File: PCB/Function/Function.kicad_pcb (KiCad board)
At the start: 2 copper layers, 101.6 x 152.4 mm, 12 parts

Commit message: Update Function.kicad_sch
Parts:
- removed J**11, J**12: Pomona_1581, 5Y:Pomona-1581
- moved J**3 56.8 mm to (38.1, 63.5)
- moved J**7 56.8 mm to (38.1, 88.9)
- moved J**4 56.8 mm to (63.5, 63.5)
- moved J**8 56.8 mm to (63.5, 88.9)
- moved J**5 50.8 mm to (88.9, 63.5)
- moved J**9 50.8 mm to (88.9, 88.9)
- moved J**10 50.8 mm to (114.3, 88.9)
- moved J**6 50.8 mm to (114.3, 63.5)
- moved J**2 25.4 mm to (88.9, 38.1)
- moved J**1 25.4 mm to (63.5, 38.1)
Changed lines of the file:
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@@
 	(net 9 "unconnected-(J**9-Pad1)")
 	(net 10 "unconnected-(J**10-Pad1)")
-	(net 11 "unconnected-(J**11-Pad1)")
-	(net 12 "unconnected-(J**12-Pad1)")
-	(footprint "5Y:Pomona-1581"
-		(layer "F.Cu")
-		(at 114.3 63.5)
+	(footprint "5Y:Pomona-1581"
+		(layer "F.Cu")
+		(at 63.5 88.9)
 		(descr "4mm banana connector")
 		(tags "jack")
@@
 	(footprint "5Y:Pomona-1581"
 		(layer "F.Cu")
-		(at 38.1 63.5)
+		(at 88.9 63.5)
 		(descr "4mm banana connector")
 		(tags "jack")
@@
 	(footprint "5Y:Pomona-1581"
 		(layer "F.Cu")
-		(at 63.5 88.9)
+		(at 114.3 88.9)
 		(descr "4mm banana connector")
 		(tags "jack")
@@
 	(footprint "5Y:Pomona-1581"
 		(layer "F.Cu")
-		(at 63.5 38.1)
+		(at 88.9 38.1)
 		(descr "4mm banana connector")
 		(tags "jack")
@@
 	(footprint "5Y:Pomona-1581"
 		(layer "F.Cu")
-		(at 88.9 88.9)
-		(descr "4mm banana connector")
-		(tags "jack")
-		(property "Reference" "J**11"
-			(at 0 -0.5 0)
-			(unlocked yes)
-			(layer "F.SilkS")
-			(hide yes)
-			(effects
-				(font
-					(size 1 1)
-					(thickness 0.1)
-				)
-			)
-		)
-		(property "Value" "Pomona_1581"
-			(at 0 1 0)
-			(unlocked yes)
-			(layer "F.Fab")
-			(hide yes)
-			(effects
-				(font
-					(size 1 1)
-					(thickness 0.15)
-				)
-			)
-		)
-		(property "Datasheet" "~"
-			(at 0 0 0)
-			(unlocked yes)
-			(layer "F.Fab")
-			(hide yes)
-			(effects
-				(font
-					(size 1 1)
-					(thickness 0.15)
-				)
-			)
-		)
-		(property "Description" "4mm banana jack"
-			(at 0 0 0)
-			(unlocked yes)
-			(layer "F.Fab")
-			(hide yes)
-			(effects
-				(font
-					(size 1 1)
-					(thickness 0.15)
-				)
-			)
-		)
-		(property ki_fp_filters "Pin*")
-		(sheetname "/")
-		(sheetfile "Function.kicad_sch")
-		(attr through_hole exclude_from_bom)
-		(fp_circle
-			(center 0 0)
-			(end 3.175 0)
-			(stroke
-				(width 0.2)
-				(type default)
-			)
-			(fill no)
-			(layer "F.Cu")
-		)
-		(pad "1" thru_hole circle
-			(at 0 0)
-			(size 9.53 9.53)
-			(drill 6.35)
-			(layers "*.Cu" "*.Mask")
-			(remove_unused_layers no)
-			(net 11 "unconnected-(J**11-Pad1)")
-			(pintype "passive")
-			(teardrops
-				(best_length_ratio 0.5)
-				(max_length 1)
-				(best_width_ratio 1)
-				(max_width 2)
-				(curved_edges no)
-				(filter_ratio 0.9)
-				(enabled yes)
-				(allow_two_segments yes)
-				(prefer_zone_connections yes)
-			)
-		)
-		(embedded_fonts no)
-	)
-	(footprint "5Y:Pomona-1581"
-		(layer "F.Cu")
-		(at 63.5 63.5)
+		(at 114.3 63.5)
 		(descr "4mm banana connector")
 		(tags "jack")
@@
 	(footprint "5Y:Pomona-1581"
 		(layer "F.Cu")
-		(at 88.9 63.5)
+		(at 38.1 88.9)
 		(descr "4mm banana connector")
 		(tags "jack")
@@
 	(footprint "5Y:Pomona-1581"
 		(layer "F.Cu")
-		(at 38.1 88.9)
+		(at 88.9 88.9)
 		(descr "4mm banana connector")
 		(tags "jack")
@@
 	(footprint "5Y:Pomona-1581"
 		(layer "F.Cu")
-		(at 114.3 38.1)
+		(at 63.5 63.5)
 		(descr "4mm banana connector")
 		(tags "jack")
@@
 	(footprint "5Y:Pomona-1581"
 		(layer "F.Cu")
-		(at 38.1 38.1)
+		(at 63.5 38.1)
 		(descr "4mm banana connector")
 		(tags "jack")
@@
 	(footprint "5Y:Pomona-1581"
 		(layer "F.Cu")
-		(at 114.3 88.9)
-		(descr "4mm banana connector")
-		(tags "jack")
-		(property "Reference" "J**12"
-			(at 0 -0.5 0)
-			(unlocked yes)
-			(layer "F.SilkS")
-			(hide yes)
-			(effects
-				(font
-					(size 1 1)
-					(thickness 0.1)
-				)
-			)
-		)
-		(property "Value" "Pomona_1581"
-			(at 0 1 0)
-			(unlocked yes)
-			(layer "F.Fab")
-			(hide yes)
-			(effects
-				(font
-					(size 1 1)
-					(thickness 0.15)
-				)
-			)
-		)
-		(property "Datasheet" "~"
-			(at 0 0 0)
-			(unlocked yes)
-			(layer "F.Fab")
-			(hide yes)
-			(effects
-				(font
-					(size 1 1)
-					(thickness 0.15)
-				)
-			)
-		)
-		(property "Description" "4mm banana jack"
-			(at 0 0 0)
-			(unlocked yes)
-			(layer "F.Fab")
-			(hide yes)
-			(effects
-				(font
-					(size 1 1)
-					(thickness 0.15)
-				)
-			)
-		)
-		(property ki_fp_filters "Pin*")
-		(sheetname "/")
-		(sheetfile "Function.kicad_sch")
-		(attr through_hole exclude_from_bom)
-		(fp_circle
-			(center 0 0)
-			(end 3.175 0)
-			(stroke
-				(width 0.2)
-				(type default)
-			)
-			(fill no)
-			(layer "F.Cu")
-		)
-		(pad "1" thru_hole circle
-			(at 0 0)
-			(size 9.53 9.53)
-			(drill 6.35)
-			(layers "*.Cu" "*.Mask")
-			(remove_unused_layers no)
-			(net 12 "unconnected-(J**12-Pad1)")
-			(pintype "passive")
-			(teardrops
-				(best_length_ratio 0.5)
-				(max_length 1)
-				(best_width_ratio 1)
-				(max_width 2)
-				(curved_edges no)
-				(filter_ratio 0.9)
-				(enabled yes)
-				(allow_two_segments yes)
-				(prefer_zone_connections yes)
-			)
-		)
-		(embedded_fonts no)
-	)
-	(footprint "5Y:Pomona-1581"
-		(layer "F.Cu")
-		(at 88.9 38.1)
-		(descr "4mm banana connector")
-		(tags "jack")
+		(at 38.1 63.5)
+		(descr "4mm banana connector")
+		(tags "jack")

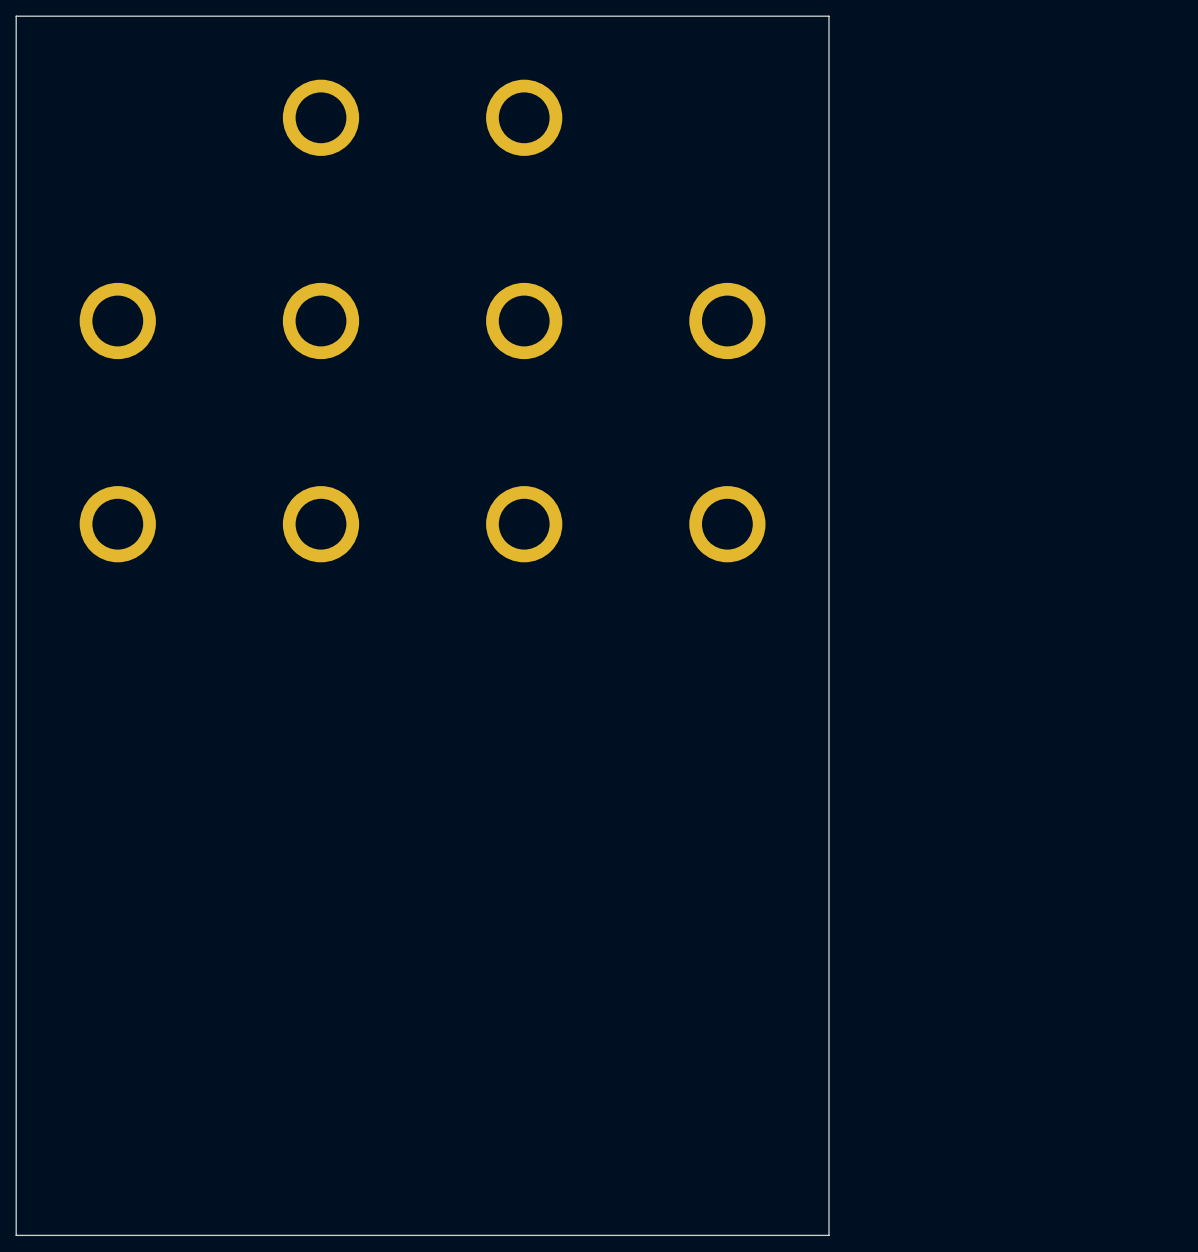
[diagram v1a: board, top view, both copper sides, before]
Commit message: Update simulation
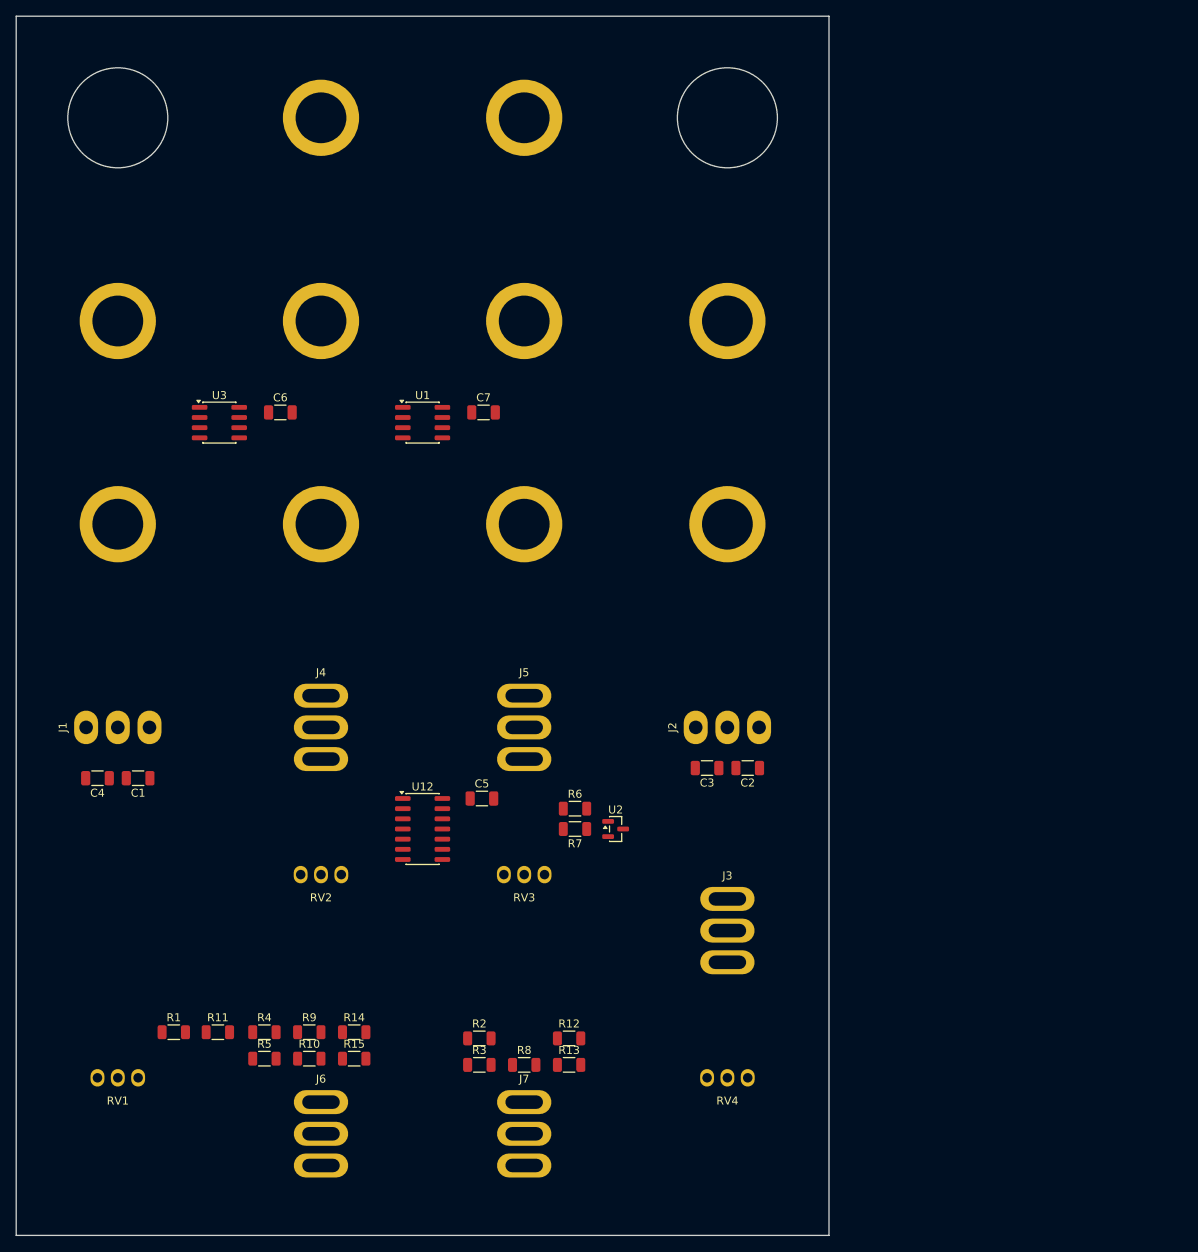
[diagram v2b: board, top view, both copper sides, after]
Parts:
- added C1: 4u7, Capacitor_SMD:C_1206_3216Metric, F.Cu at (40.6, 120.7)
- added C2: 4u7, Capacitor_SMD:C_1206_3216Metric, F.Cu at (116.8, 119.4)
- added C3: 4u7, Capacitor_SMD:C_1206_3216Metric, F.Cu at (111.8, 119.4)
- added C4: 4u7, Capacitor_SMD:C_1206_3216Metric, F.Cu at (35.6, 120.7)
- added C5: 100n, Capacitor_SMD:C_1206_3216Metric, F.Cu at (83.6, 123.2)
- added C6: 100n, Capacitor_SMD:C_1206_3216Metric, F.Cu at (58.4, 74.9)
- added C7: 100n, Capacitor_SMD:C_1206_3216Metric, F.Cu at (83.8, 74.9)
- added J1: MTA156-3, 5Y:MTA156-3, F.Cu at (38.1, 114.3)
- added J2: MTA156-3, 5Y:MTA156-3, F.Cu at (114.3, 114.3)
- added J3: MN12, 5Y:MBNF15, F.Cu at (114.3, 139.7)
- added J4: MN12, 5Y:MBNF15, F.Cu at (63.5, 114.3)
- added J5: MN12, 5Y:MBNF15, F.Cu at (88.9, 114.3)
- added J6: MBNF15, 5Y:MBNF15, F.Cu at (63.5, 165.1)
- added J7: MBNF15, 5Y:MBNF15, F.Cu at (88.9, 165.1)
- added R1: 4K7, Resistor_SMD:R_1206_3216Metric, F.Cu at (45.1, 152.4)
- added R10: 100K, Resistor_SMD:R_1206_3216Metric, F.Cu at (62.0, 155.7)
- added R11: 100K, Resistor_SMD:R_1206_3216Metric, F.Cu at (50.6, 152.4)
- added R12: 470R, Resistor_SMD:R_1206_3216Metric, F.Cu at (94.5, 153.2)
- added R13: 150K, Resistor_SMD:R_1206_3216Metric, F.Cu at (94.5, 156.5)
- added R14: 4K7, Resistor_SMD:R_1206_3216Metric, F.Cu at (67.6, 152.4)
- added R15: 4K7, Resistor_SMD:R_1206_3216Metric, F.Cu at (67.6, 155.7)
- added R2: 680K, Resistor_SMD:R_1206_3216Metric, F.Cu at (83.3, 153.2)
- added R3: 10K, Resistor_SMD:R_1206_3216Metric, F.Cu at (83.3, 156.5)
- added R4: 100K, Resistor_SMD:R_1206_3216Metric, F.Cu at (56.4, 152.4)
- added R5: 10K, Resistor_SMD:R_1206_3216Metric, F.Cu at (56.4, 155.7)
- added R6: 100K, Resistor_SMD:R_1206_3216Metric, F.Cu at (95.2, 124.5)
- added R7: 100K, Resistor_SMD:R_1206_3216Metric, F.Cu at (95.2, 127.0)
- added R8: 680K, Resistor_SMD:R_1206_3216Metric, F.Cu at (88.9, 156.5)
- added R9: 100K, Resistor_SMD:R_1206_3216Metric, F.Cu at (62.0, 152.4)
- added RV1: Bourns_51, 5Y:Bourns_51, F.Cu at (38.1, 165.1)
- added RV2: Bourns_51, 5Y:Bourns_51, F.Cu at (63.5, 139.7)
- added RV3: Bourns_51, 5Y:Bourns_51, F.Cu at (88.9, 139.7)
- added RV4: Bourns_51, 5Y:Bourns_51, F.Cu at (114.3, 165.1)
- added U1: AD823, 5Y:SOIC-8, F.Cu at (76.2, 76.2)
- added U12: 4013, Package_SO:SOIC-14_3.9x8.7mm_P1.27mm, F.Cu at (76.2, 127.0)
- added U2: ADR5045, Package_TO_SOT_SMD:SOT-23, F.Cu at (100.3, 127.0)
- added U3: AD823, 5Y:SOIC-8, F.Cu at (50.8, 76.2)
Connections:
- J**1 pad 1: unconnected-(J**1-Pad1) -> LPO
- J**10 pad 1: unconnected-(J**10-Pad1) -> HOLD_IN
- J**2 pad 1: unconnected-(J**2-Pad1) -> ENDO
- J**3 pad 1: unconnected-(J**3-Pad1) -> SIG_IN
- J**4 pad 1: unconnected-(J**4-Pad1) -> NLPO
- J**5 pad 1: unconnected-(J**5-Pad1) -> LIMO
- J**6 pad 1: unconnected-(J**6-Pad1) -> TRIG_IN
- J**7 pad 1: unconnected-(J**7-Pad1) -> FREQ_IN
- J**8 pad 1: unconnected-(J**8-Pad1) -> FALL_IN
- J**9 pad 1: unconnected-(J**9-Pad1) -> RISE_IN
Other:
- outline, holes or cut-outs redrawn
